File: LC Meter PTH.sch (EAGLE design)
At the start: 39 parts, among them IC1 PIC16F628SO

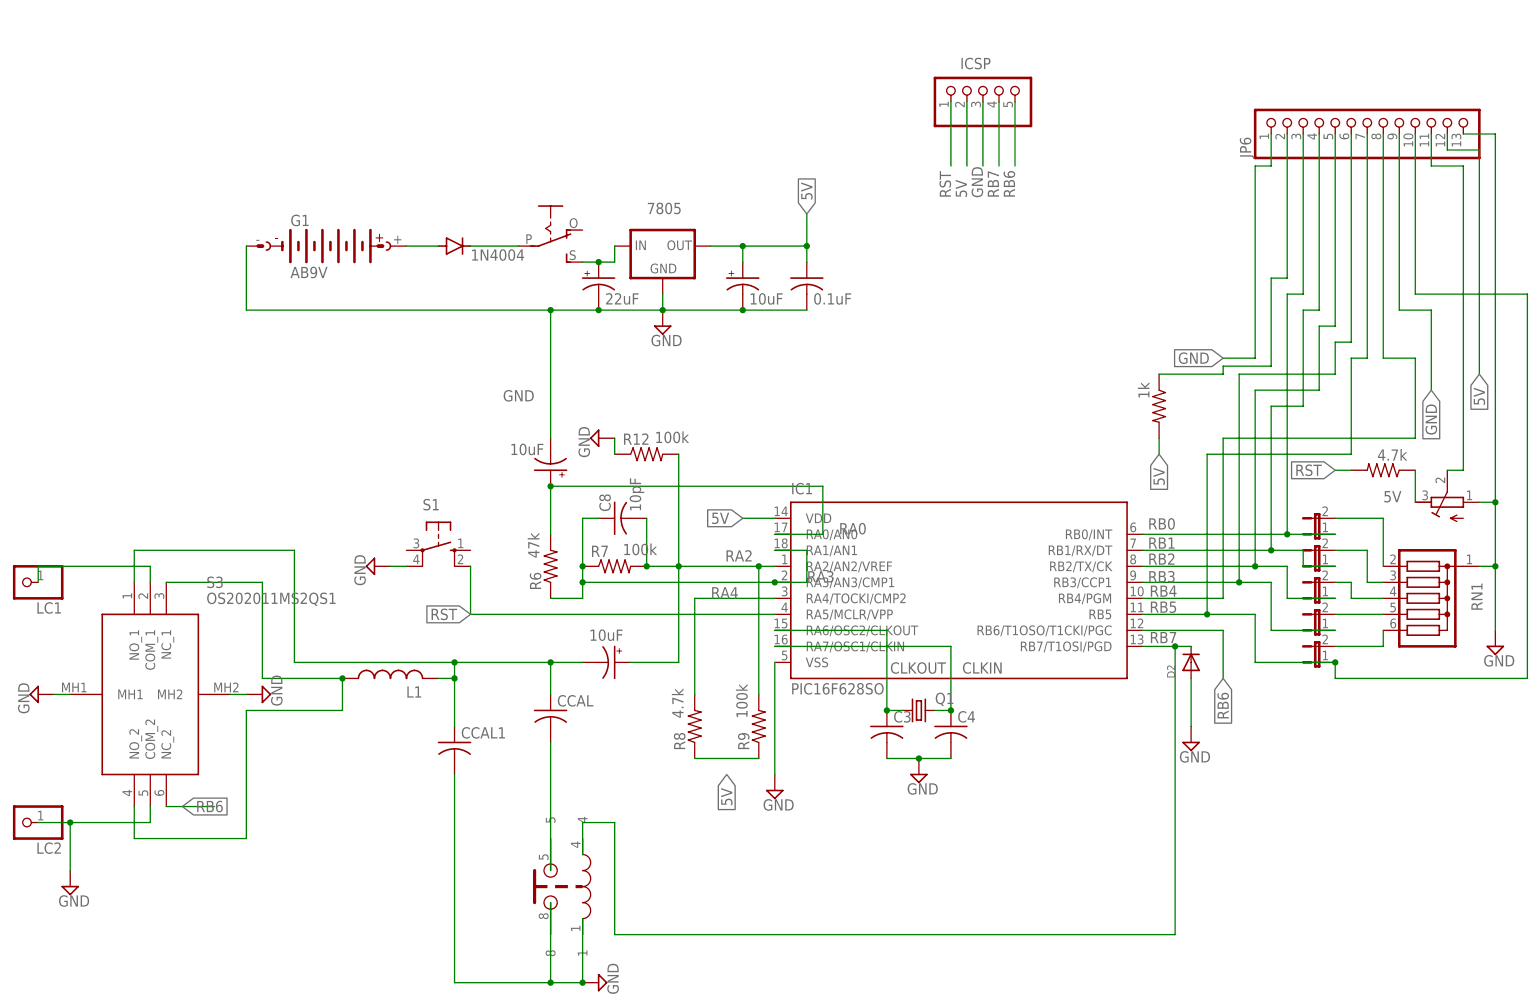
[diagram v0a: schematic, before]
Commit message: Fix for iCloud symlink issue
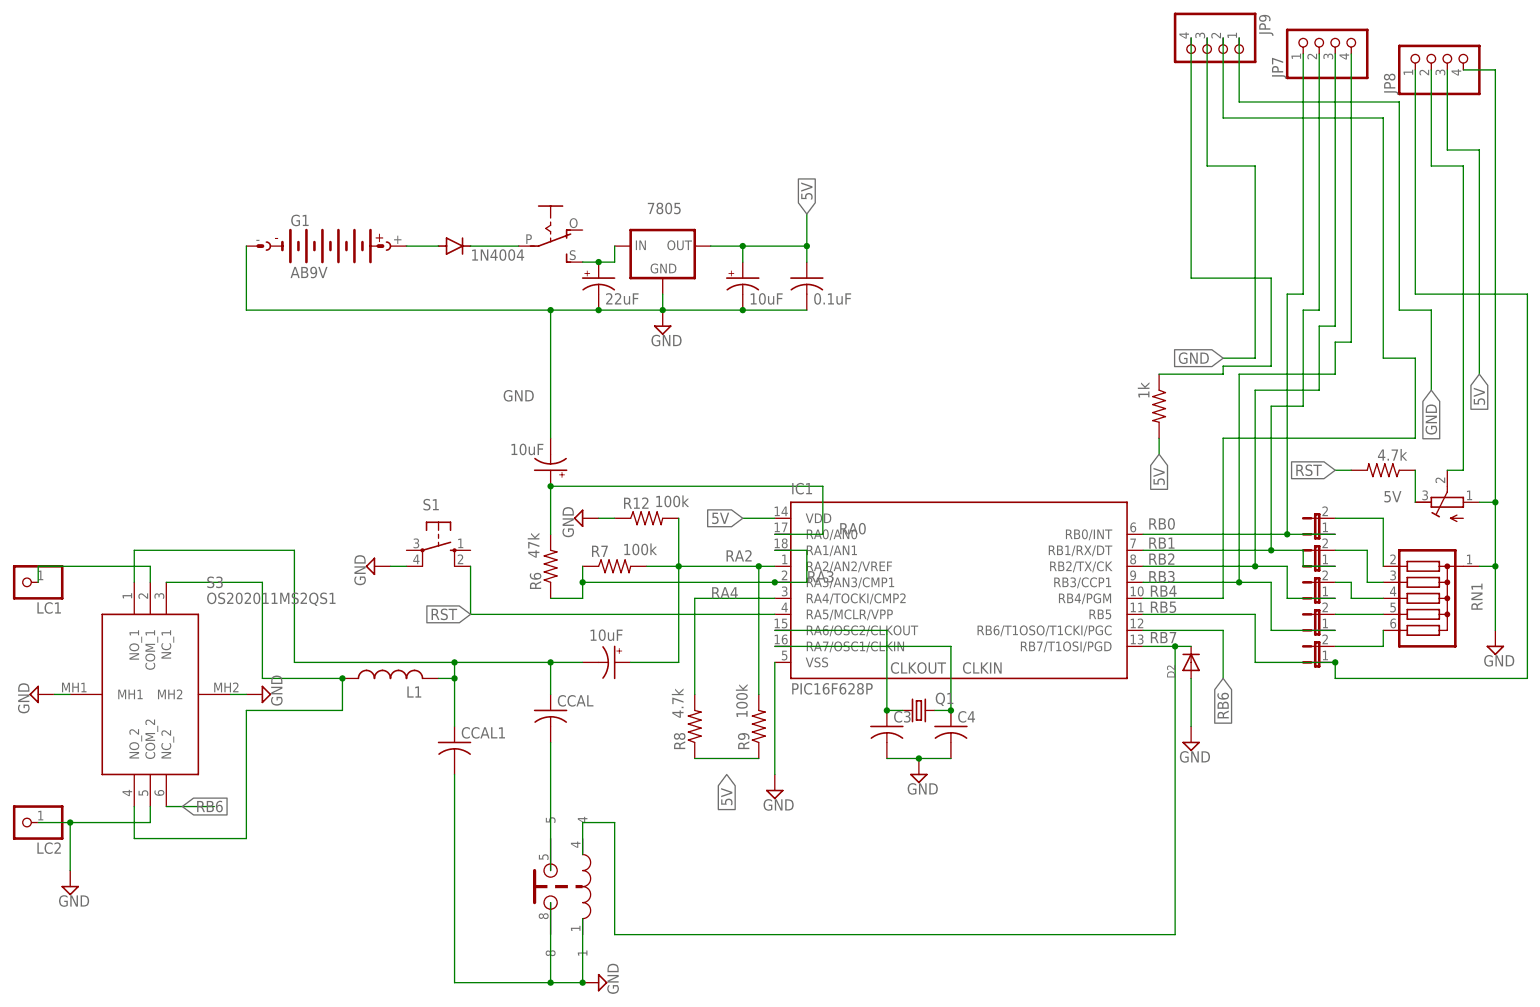
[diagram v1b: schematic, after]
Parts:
- removed C8: 10pF, rcl:C-US025-024X044
- removed ICSP: (no value), pinhead:PINHD-1X5
- removed JP6: (no value), pinhead:PINHD-1X13
- added JP7, JP8, JP9: (no value), pinhead:PINHD-1X4
- C1: device adafruit:CPOL-USB/3528-21R -> adafruit:CPOL-USE2.5-7
- C2: device rcl:C-USC0603 -> rcl:C-US050-025X075
- C3, C4: device rcl:C-USC0603 -> rcl:C-US025-030X050
- IC1: value PIC16F628SO -> PIC16F628P; device microchip:PIC16F628SO -> microchip:PIC16F628P
- R1: device rcl:R-US_R0603 -> rcl:R-US_0207/7
- R10, R12, R6, R7, R8, R9: device rcl:R-US_0204/7 -> rcl:R-US_0207/7
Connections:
- net 5V: now also JP8.3; no longer ICSP.2, JP6.12
- net GND: now also JP8.4, JP9.1, JP9.3; no longer ICSP.3, JP6.1, JP6.13, JP6.9
- net N$23: now also JP8.2; no longer JP6.11
- net N$31: now also JP9.4; no longer JP6.2
- net RA2: no longer C8.2
- net RA3: no longer C8.1
- net RB0: now also JP7.1; no longer JP6.3
- net RB1: now also JP7.2; no longer JP6.4
- net RB2: now also JP7.3; no longer JP6.5
- net RB3: now also JP7.4; no longer JP6.6
- net RB4: now also JP9.2; no longer JP6.8
- net RB5: now also JP8.1; no longer JP6.10, JP6.7
- net RB6: no longer ICSP.5
- net RB7: no longer ICSP.4
- net RST: no longer ICSP.1
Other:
- moved on the sheet: R12
